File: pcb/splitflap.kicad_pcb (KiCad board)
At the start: 2 copper layers, 96 x 54 mm, 70 parts, among them J1 Motor A, J10 Hall C, J11 Hall-D, J12 Conn_01x03, J13 Conn_01x03, J14 Conn_01x03, J15 Conn_01x03, J2 Motor B, J3 Motor C, J4 Motor D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

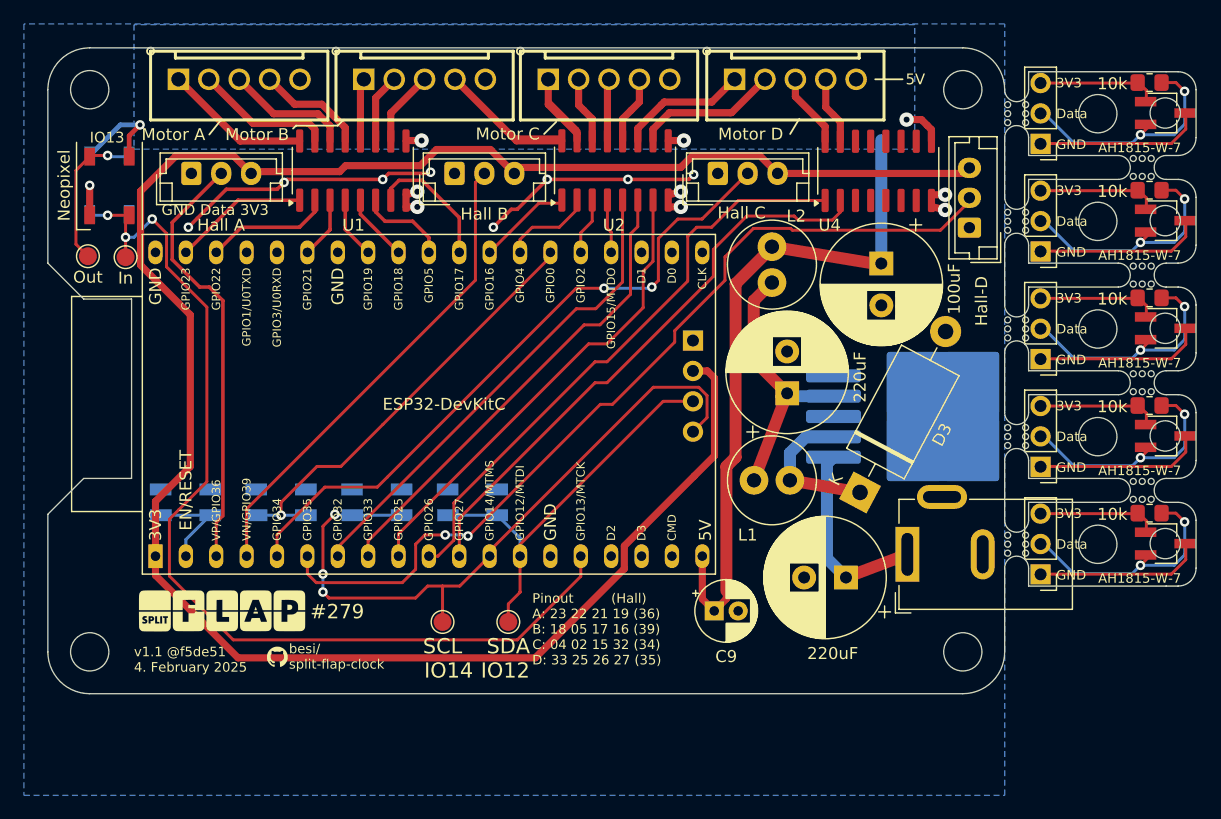
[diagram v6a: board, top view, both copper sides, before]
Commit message: Rework 3
Now the signal flow is the recommended way: inputs far away from power outputs. The Hall sensor connectors have been moved to the front of the PCB.
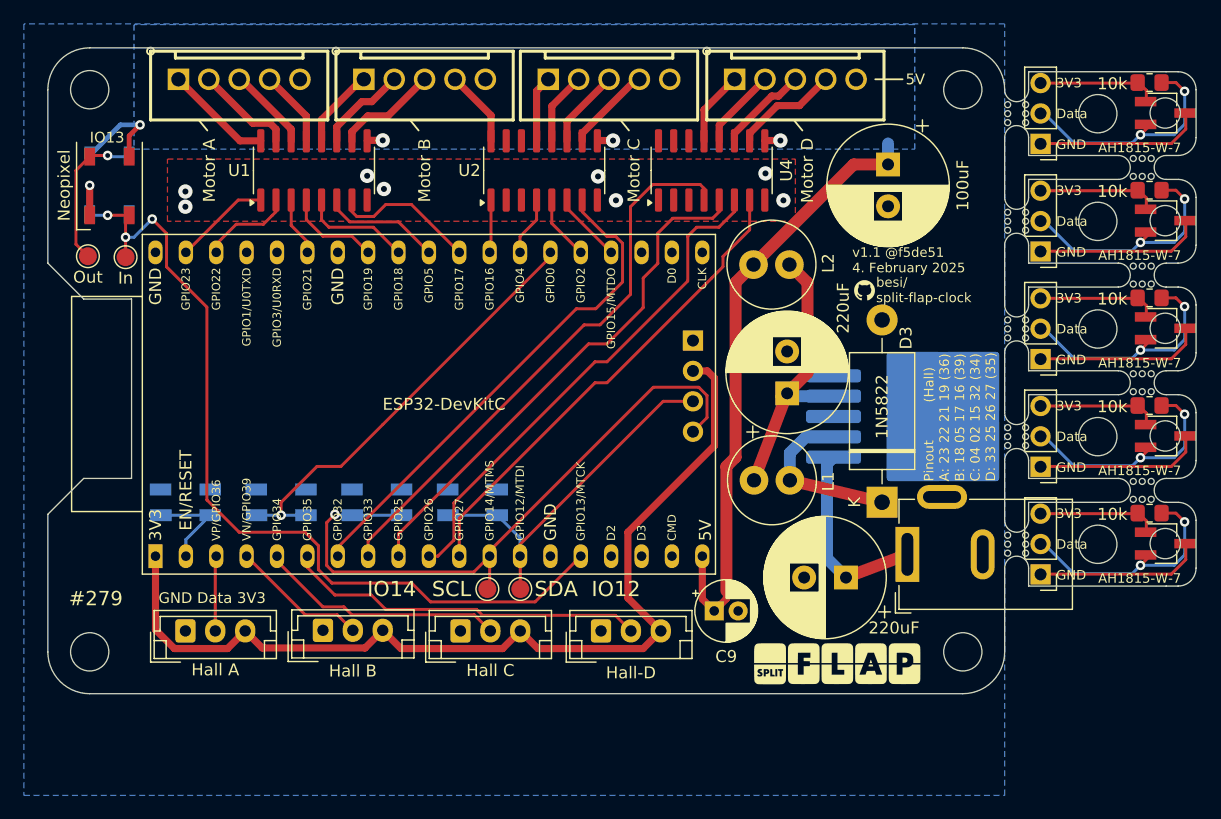
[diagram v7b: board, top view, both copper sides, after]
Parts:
- moved G*** 57.9 mm to (153.2, 105.2)
- moved G*** 51.6 mm to (151.0, 136.5)
- moved J11 45.7 mm to (131.2, 133.8), turned to 0 degrees
- moved J10 43.9 mm to (119.5, 133.8)
- moved J9 39.8 mm to (108.0, 133.7)
- moved J8 38.3 mm to (96.5, 133.8)
- moved OSHW1 22.5 mm to (153.0, 134.8)
- moved U4 13.9 mm to (140.5, 95.2)
- moved C8 8.30 mm to (155.2, 94.8)
- moved U2 5.92 mm to (126.5, 95.2)
- moved TP4 4.65 mm to (121.8, 130.2)
- moved U1 3.25 mm to (107.2, 95.2)
- moved TP3 2.93 mm to (124.5, 130.2)
- moved L2 2.09 mm to (147.0, 103.1), turned to 180 degrees
- moved D3 2.01 mm to (154.8, 123.0), turned to 90 degrees
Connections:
- J3 pad 1: Net-(U2-O2) -> Net-(U2-O4)
- J3 pad 2: Net-(U2-O3) -> Net-(U2-O5)
- J3 pad 3: Net-(U2-O4) -> Net-(U2-O6)
- J3 pad 4: Net-(U2-O5) -> Net-(U2-O7)
- J4 pad 1: Net-(U2-O6) -> Net-(U4-O4)
- J4 pad 2: Net-(U2-O7) -> Net-(U4-O5)
- J4 pad 3: Net-(U4-O1) -> Net-(U4-O6)
- J4 pad 4: Net-(U4-O2) -> Net-(U4-O7)
- U2 pad 14: Net-(U2-O3) -> unconnected-(U2-O3-Pad14)
- U2 pad 15: Net-(U2-O2) -> unconnected-(U2-O2-Pad15)
- U2 pad 2: GPIO4 -> unconnected-(U2-I2-Pad2)
- U2 pad 3: GPIO2 -> unconnected-(U2-I3-Pad3)
- U2 pad 4: GPIO15 -> GPIO4
- U2 pad 5: GPIO32 -> GPIO2
- U2 pad 6: GPIO33 -> GPIO15
- U2 pad 7: GPIO25 -> GPIO32
- U4 pad 1: GPIO26 -> unconnected-(U4-I1-Pad1)
- U4 pad 10: unconnected-(U4-O7-Pad10) -> Net-(U4-O7)
- U4 pad 11: unconnected-(U4-O6-Pad11) -> Net-(U4-O6)
- U4 pad 12: unconnected-(U4-O5-Pad12) -> Net-(U4-O5)
- U4 pad 13: unconnected-(U4-O4-Pad13) -> Net-(U4-O4)
- U4 pad 15: Net-(U4-O2) -> unconnected-(U4-O2-Pad15)
- U4 pad 16: Net-(U4-O1) -> unconnected-(U4-O1-Pad16)
- U4 pad 2: GPIO27 -> unconnected-(U4-I2-Pad2)
- U4 pad 4: unconnected-(U4-I4-Pad4) -> GPIO33
- U4 pad 5: unconnected-(U4-I5-Pad5) -> GPIO25
- U4 pad 6: unconnected-(U4-I6-Pad6) -> GPIO26
- U4 pad 7: unconnected-(U4-I7-Pad7) -> GPIO27
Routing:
- net +3V3: track 175.5 -> 80.6 mm
- net GND: track 49.9 -> 2.50 mm, vias 15 -> 9
- net GPI35: track 73.8 -> 30.2 mm, vias 2 -> 0
- net GPI34: track 55.7 -> 20.7 mm, vias 2 -> 0
- net GPI36: track 36.2 -> 6.28 mm
- net GPI39: track 40.2 -> 11.4 mm
- net Net-(U2-O7): track 23.9 -> 7.28 mm
- net Net-(U2-O1): track 22.0 -> 6.39 mm
- net Net-(U2-O2): track 12.0 -> 0.00 mm
- net GPIO13: track 83.4 -> 72.8 mm
- net Net-(U4-O7): track 0.00 -> 8.86 mm
- net Net-(U2-O3): track 8.22 -> 0.00 mm
- net GPIO27: track 48.2 -> 40.4 mm
- net +5V: track 73.1 -> 65.3 mm
- net Net-(U4-O6): track 0.00 -> 7.59 mm
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- added copper zone on F.Cu, net GND

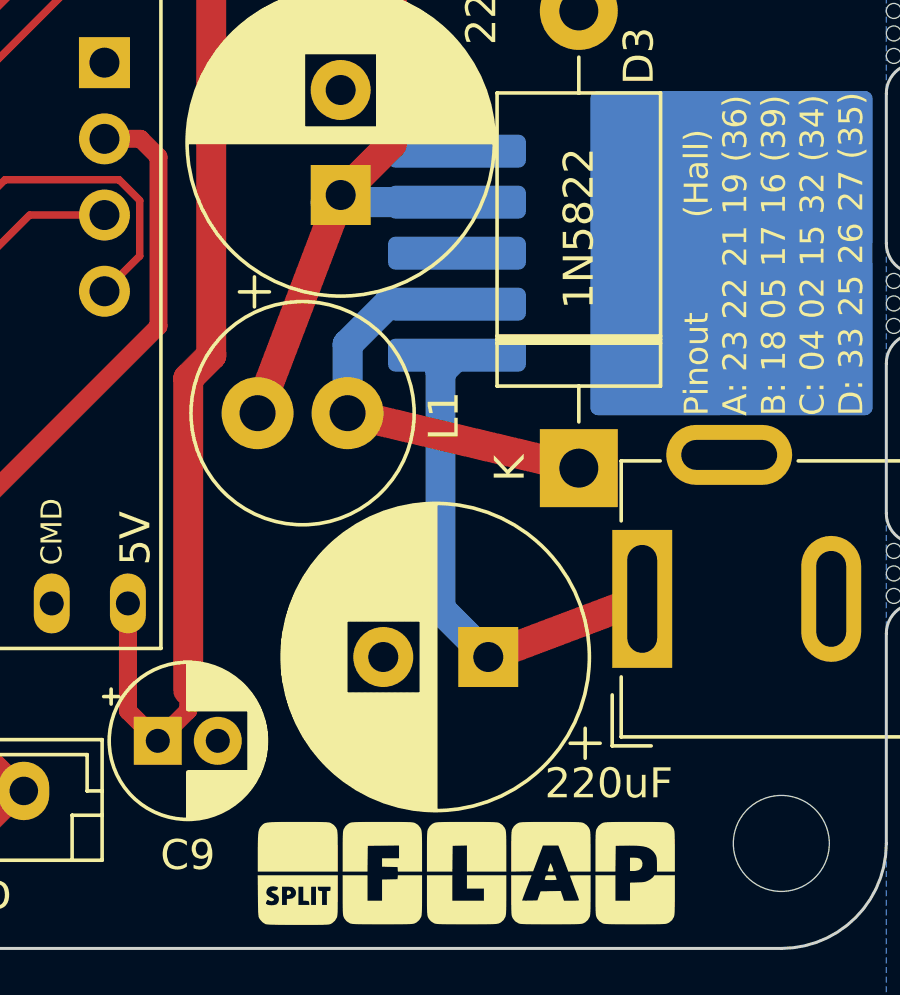
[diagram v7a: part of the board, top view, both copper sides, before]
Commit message: Rework 4
The trace from the 12V input capacitor to the switcher ran on the bottom layer, making for a rather deep cut in the ground plane. This trace has been partially moved to the top layer, avoiding the cut.
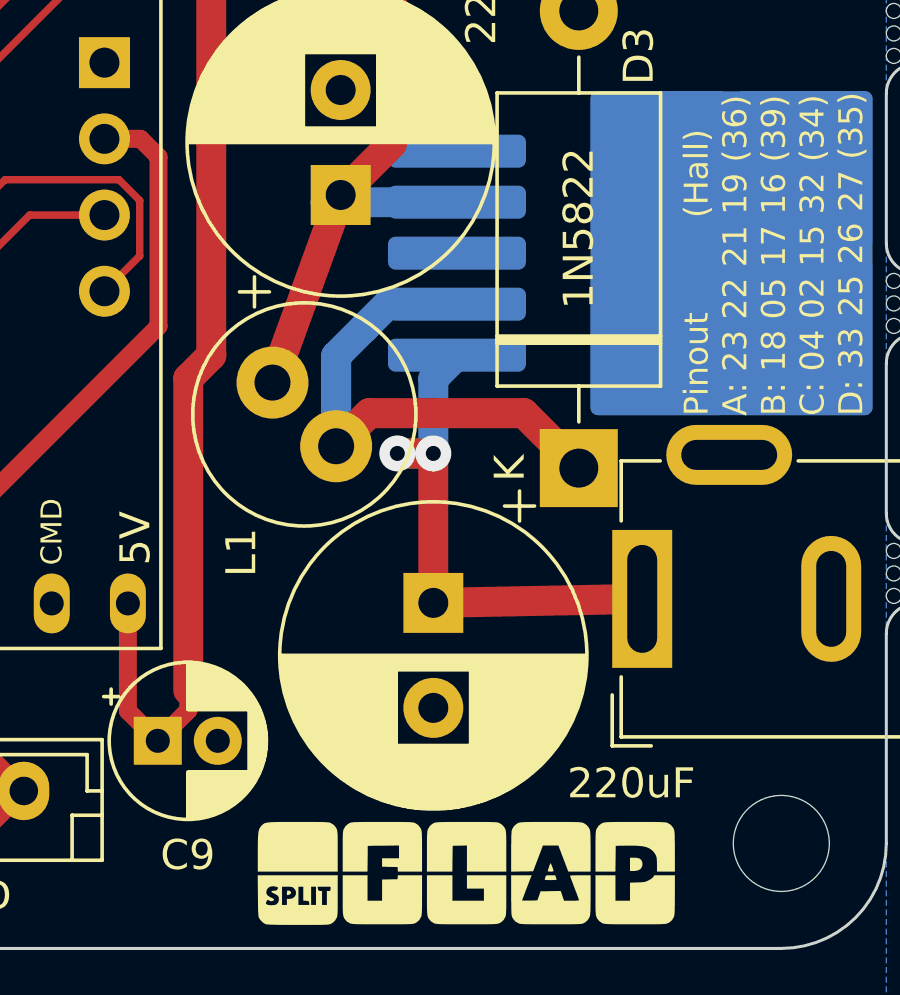
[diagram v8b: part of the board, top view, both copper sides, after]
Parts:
- moved C6 2.57 mm to (149.9, 127.5), turned to -90 degrees
- moved L1 1.17 mm to (146.7, 122.3), turned to 135 degrees
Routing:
- net /POW_OUT: track 14.4 -> 17.1 mm
- net +12V: track 16.6 -> 18.1 mm, vias 0 -> 2
- net /POW_FB: track 23.9 -> 22.7 mm
